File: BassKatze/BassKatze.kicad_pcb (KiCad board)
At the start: 2 copper layers, 55 x 54.9 mm, 52 parts, among them J1 Conn_01x02_Female, Q1 IRF7404, Q2 BSS138, SW1 SW_Push, U1 ATmega328-AU, U2 MSGEQ7, U3 TP4056

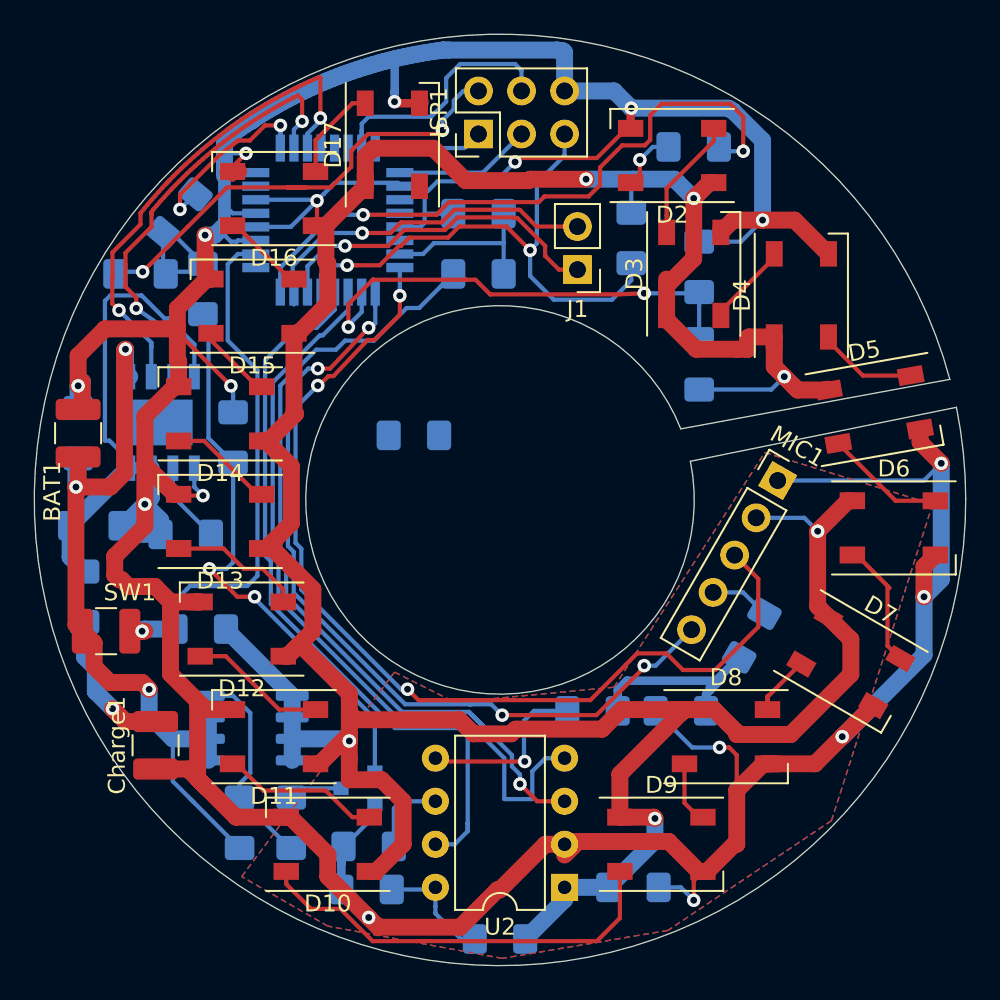
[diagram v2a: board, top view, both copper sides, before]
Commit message: use voltage converters to prevent isp burnout
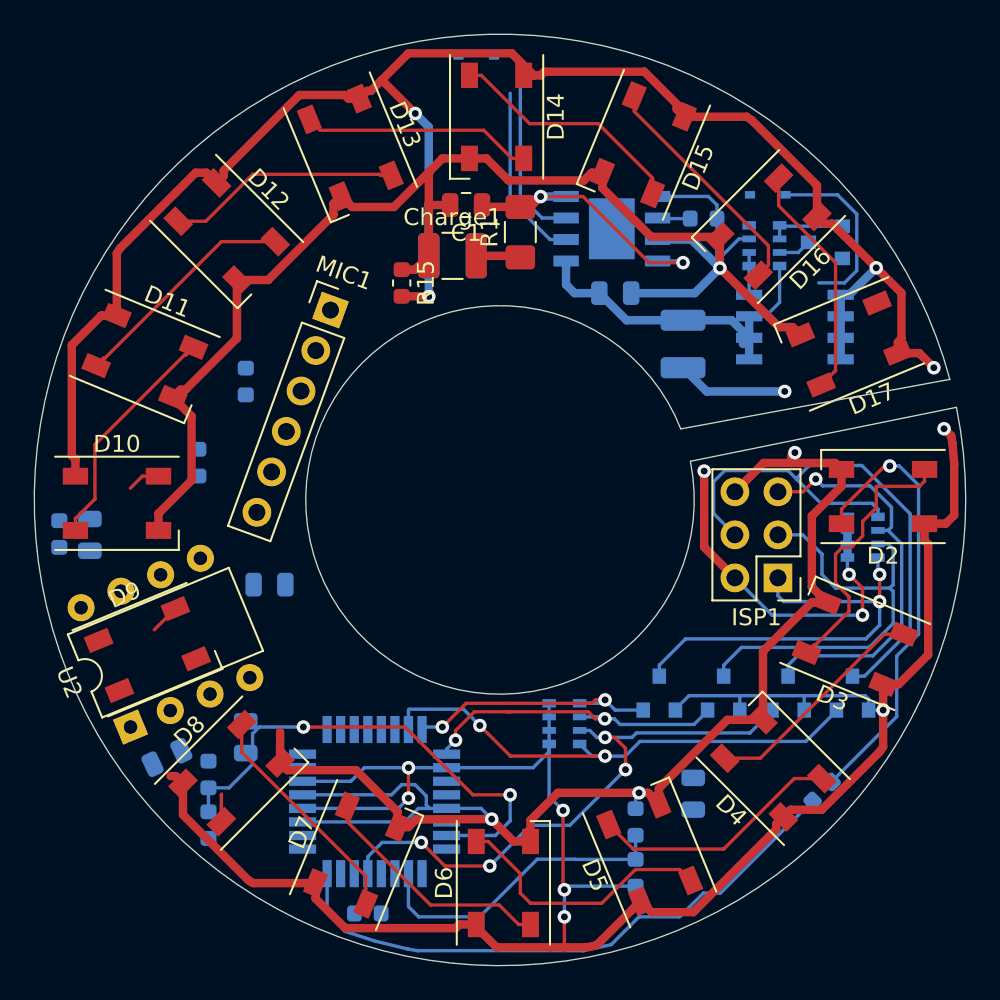
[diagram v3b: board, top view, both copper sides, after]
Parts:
- removed R11, R12, R13, R4: 10KOhm, Resistor_SMD:R_1206_3216Metric_Pad1.42x1.75mm_HandSolder
- added Q3: BSS138, Package_TO_SOT_SMD:SOT-23, B.Cu at (147.8, 138.4)
- added Q4: BSS138, Package_TO_SOT_SMD:SOT-23, B.Cu at (144.0, 138.4)
- added Q5: BSS138, Package_TO_SOT_SMD:SOT-23, B.Cu at (136.4, 138.4)
- added Q6: BSS138, Package_TO_SOT_SMD:SOT-23, B.Cu at (140.2, 138.4)
- added RN1: R_Pack04, Resistor_SMD:R_Array_Convex_4x0603, B.Cu at (148.4, 129.2)
- added RN2: R_Pack0410K, Resistor_SMD:R_Array_Convex_4x0603, B.Cu at (142.6, 112.0)
- added RN3: R_Pack04, Resistor_SMD:R_Array_Convex_4x0603, B.Cu at (130.8, 140.2)
- BAT1, SW1: moved to B.Cu
- C1: footprint Resistor_SMD:R_1206_3216Metric_Pad1.42x1.75mm_HandSolder -> Capacitor_SMD:C_0805_2012Metric; moved to F.Cu
- C2, C3, C4, C5, C6: footprint Resistor_SMD:R_1206_3216Metric_Pad1.42x1.75mm_HandSolder -> Capacitor_SMD:C_0805_2012Metric
- D1, D18, D19: footprint Diode_SMD:D_1206_3216Metric_Pad1.42x1.75mm_HandSolder -> Diode_SMD:D_SOD-323
- J1: footprint Connector_PinHeader_2.54mm:PinHeader_1x02_P2.54mm_Vertical -> Resistor_SMD:R_0603_1608Metric; moved to B.Cu
- MIC1: footprint Connector_PinHeader_2.54mm:PinHeader_1x05_P2.54mm_Vertical -> Connector_PinHeader_2.54mm:PinHeader_1x06_P2.54mm_Vertical
- R1: value 0.4Ohm -> 0.2Ohm; moved to F.Cu
- R10, R14, R2, R3, R6, R7, R8, R9, RProg1: footprint Resistor_SMD:R_1206_3216Metric_Pad1.42x1.75mm_HandSolder -> Resistor_SMD:R_0603_1608Metric
- R15: footprint Resistor_SMD:R_1206_3216Metric_Pad1.42x1.75mm_HandSolder -> Resistor_SMD:R_0603_1608Metric; moved to F.Cu
- R5: footprint Resistor_SMD:R_1206_3216Metric_Pad1.42x1.75mm_HandSolder -> Resistor_SMD:R_0805_2012Metric
- moved Q2 42.4 mm to (146.2, 111.8)
- moved J1 40.0 mm to (119.2, 151.4)
- moved Q1 39.9 mm to (144.4, 116.8)
- moved R9 39.4 mm to (109.8, 146.2), turned to 270 degrees
- moved R14 38.8 mm to (146.0, 144.2), turned to 225 degrees
- moved D19 37.3 mm to (142.8, 109.0), turned to 0 degrees
- moved BAT1 36.1 mm to (137.8, 117.8), turned to 90 degrees
- moved RProg1 35.8 mm to (139.0, 110.4), turned to 0 degrees
- moved R3 35.3 mm to (101.0, 129.0), turned to 90 degrees
- moved U1 34.4 mm to (119.6, 144.8)
- moved R6 34.2 mm to (109.2, 124.8), turned to 90 degrees
- moved Charge1 33.8 mm to (124.2, 112.6), turned to 0 degrees
- moved R10 33.6 mm to (109.8, 143.2), turned to 270 degrees
- moved R1 33.5 mm to (128.2, 111.2)
- moved R5 33.0 mm to (138.4, 144.3)
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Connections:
- ISP1 pad 1: MISO -> MISO_5V
- ISP1 pad 3: SCK -> SCK_5V
- ISP1 pad 4: MOSI -> MOSI_5V
- ISP1 pad 5: Reset -> Reset_5V
- U1 pad 1: Net-(U1-Pad1) -> Free1
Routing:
- net BAT-: track 285.3 -> 182.1 mm, vias 16 -> 5
- net Gain_Select: track 59.3 -> 0.00 mm, vias 3 -> 0
- net RAW_Spectrum: track 51.8 -> 0.00 mm, vias 1 -> 0
- net Attack_Select: track 50.4 -> 0.00 mm, vias 4 -> 0
- net EQ_Band: track 45.3 -> 0.00 mm
- net EQ_Reset: track 43.9 -> 0.00 mm
- net MOSI_5V: track 0.00 -> 34.7 mm
- net Net-(Q2-Pad1): track 33.5 -> 4.52 mm, vias 2 -> 0
- net BAT+: track 47.7 -> 21.3 mm, vias 3 -> 0
- net SCK_5V: track 0.00 -> 25.9 mm
- net MISO_5V: track 0.00 -> 25.9 mm, vias 0 -> 2
- net Button: track 32.3 -> 7.08 mm
- net Reset_5V: track 0.00 -> 24.1 mm, vias 0 -> 1
- net Net-(D10-Pad2): track 25.1 -> 1.95 mm
- net LED1: track 3.57 -> 26.2 mm
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- removed copper zone on B.Cu, net BAT-
- removed copper zone on F.Cu, net BAT-
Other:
- net class Default: clearance 0.2 -> 0.3; trace_width 0.25 -> 0.2
- net class High added: clearance 0.3, trace_width 0.2, via_dia 0.8, via_drill 0.4
- rule trace_clearance: 0.2 -> 0.3
- board text removed: "BassKatze Rev 0.4"

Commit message: tracing of 0.8 finished
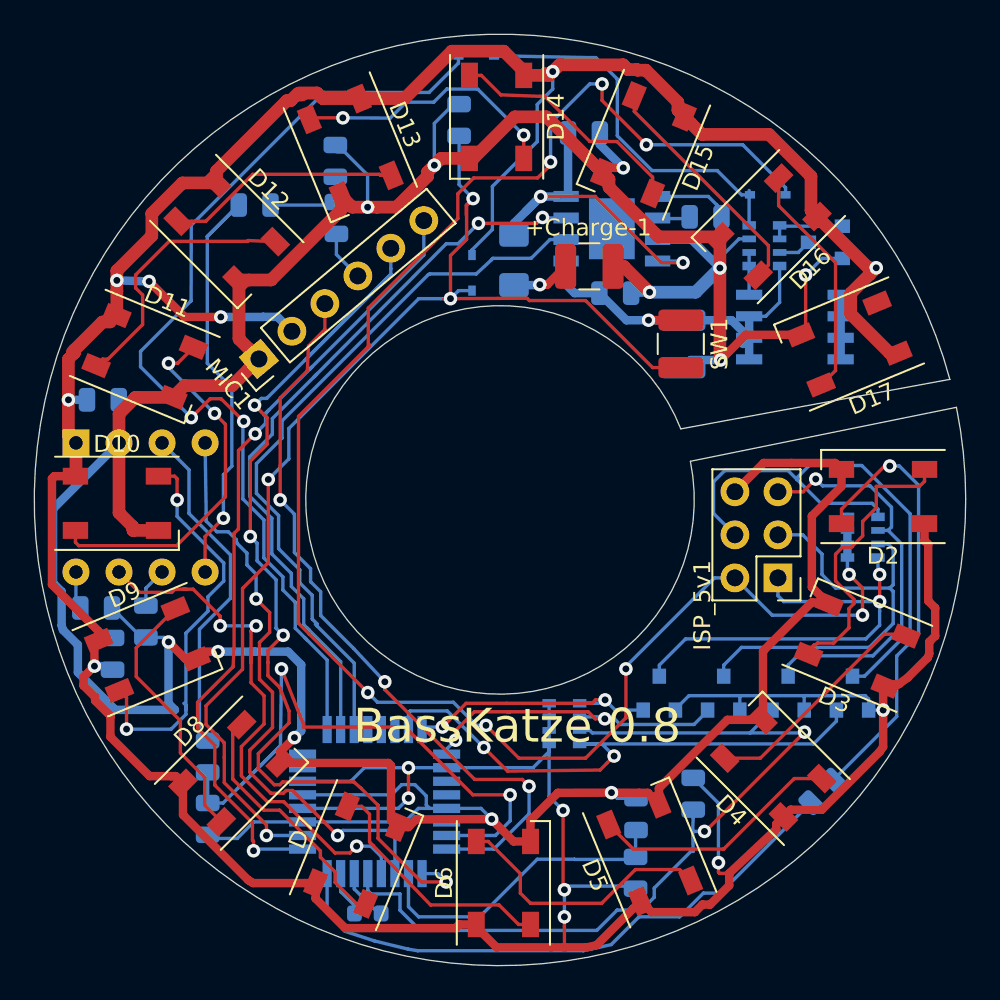
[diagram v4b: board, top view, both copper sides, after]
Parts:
- C1, R1, U2: moved to B.Cu
- R10, R14, R2, R3, R6, R7, R8, R9, RProg1: footprint Resistor_SMD:R_0603_1608Metric -> Resistor_SMD:R_0805_2012Metric
- R15: footprint Resistor_SMD:R_0603_1608Metric -> Resistor_SMD:R_0805_2012Metric; moved to B.Cu
- SW1: moved to F.Cu
- moved C3 22.4 mm to (112.5, 109.6)
- moved C5 21.4 mm to (103.6, 121.1), turned to 0 degrees
- moved U2 17.1 mm to (102.0, 123.6), turned to 270 degrees
- moved R6 16.6 mm to (117.3, 110.4), turned to 270 degrees
- moved SW1 14.4 mm to (137.7, 117.8), turned to 270 degrees
- moved R2 14.0 mm to (117.3, 107.0), turned to 270 degrees
- moved R15 10.2 mm to (124.6, 104.6)
- moved C6 9.02 mm to (106.1, 134.2)
- moved C1 8.15 mm to (132.0, 105.3), turned to 0 degrees
- moved +Charge-1 8.09 mm to (132.3, 113.2), turned to 180 degrees
- moved R3 7.73 mm to (104.1, 136.1), turned to 270 degrees
- moved D1 5.73 mm to (125.3, 113.6)
- moved MIC1 5.11 mm to (112.8, 118.7), turned to 130 degrees
- moved C4 4.33 mm to (103.2, 133.4), turned to 0 degrees
- moved R1 1.68 mm to (127.8, 112.8)
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- renumbered BAT1 to +Bat-1, Charge1 to +Charge-1, ISP1 to ISP_5v1
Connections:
- D17 pad 4: Net-(D17-Pad4) -> (no net)
- U1 pad 12: Net-(U1-Pad12) -> (no net)
- U1 pad 13: Net-(U1-Pad13) -> (no net)
- U1 pad 14: Net-(U1-Pad14) -> (no net)
- U1 pad 19: Net-(U1-Pad19) -> (no net)
- U1 pad 20: Net-(U1-Pad20) -> (no net)
- U1 pad 22: Net-(U1-Pad22) -> (no net)
- U1 pad 7: Net-(U1-Pad7) -> (no net)
- U1 pad 8: Net-(U1-Pad8) -> (no net)
- U3 pad 9: Net-(U3-Pad9) -> (no net)
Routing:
- net BAT-: track 182.1 -> 267.2 mm, vias 5 -> 12
- net 5V_Flash: track 32.2 -> 106.2 mm, vias 3 -> 8
- net Button: track 7.08 -> 71.3 mm, vias 1 -> 4
- net Attack_Select: track 0.00 -> 61.2 mm, vias 0 -> 4
- net PWR_HOLD: track 0.00 -> 58.5 mm, vias 0 -> 2
- net PWR: track 227.9 -> 282.6 mm, vias 10 -> 14
- net Free1: track 0.00 -> 47.6 mm, vias 0 -> 2
- net Gain_Select: track 0.00 -> 44.6 mm, vias 0 -> 3
- net EQ_Band: track 0.00 -> 35.2 mm, vias 0 -> 2
- net CHRG: track 10.3 -> 44.0 mm, vias 0 -> 2
- net STDBY: track 10.6 -> 42.5 mm
- net EQ_Reset: track 0.00 -> 31.9 mm, vias 0 -> 3
- net Net-(C3-Pad1): track 0.00 -> 26.3 mm, vias 0 -> 1
- net Net-(D18-Pad1): track 0.00 -> 22.5 mm
- net Net-(D10-Pad2): track 1.95 -> 24.0 mm, vias 0 -> 2
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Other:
- net class Default: clearance 0.3 -> 0.2
- rule trace_clearance: 0.3 -> 0.2
- board text added: "BassKatze 0.8"
